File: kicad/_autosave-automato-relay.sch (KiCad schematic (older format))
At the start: 39 parts, among them J1 TE-3-213598-4, J2 Screw_Terminal_01x03, J3 TE-3-213598-4, J4 Screw_Terminal_01x05, J5 TE-3-213598-4, J6 TE-3-213598-4, J7 Screw_Terminal_01x05, J8 TE-3-213598-4, K1 G5LE-14, K2 G5LE-14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

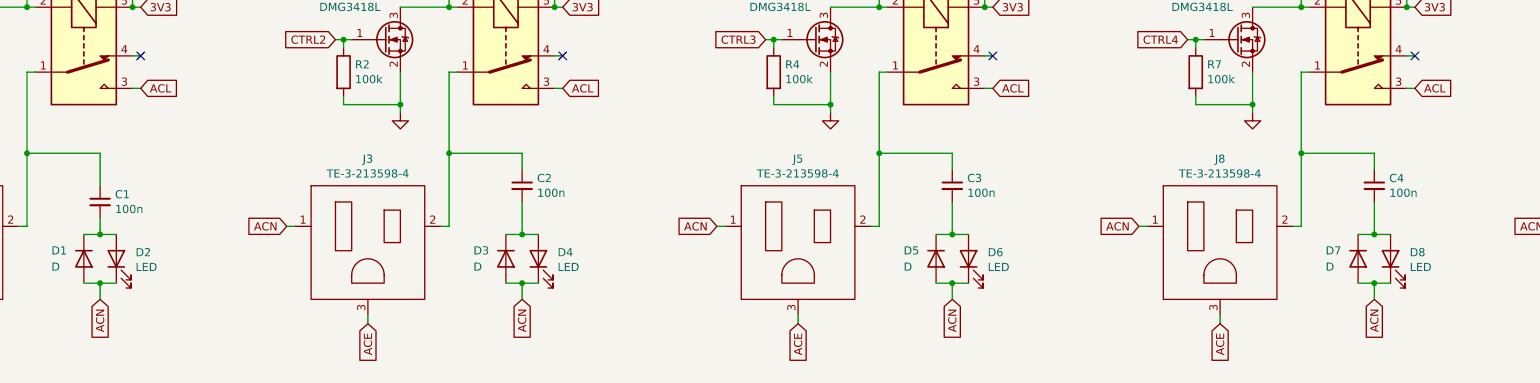
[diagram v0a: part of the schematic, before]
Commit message: Final Rev
Added varistor, poured power planes, added mounting holes, modified data headers, added space for IEC connector.
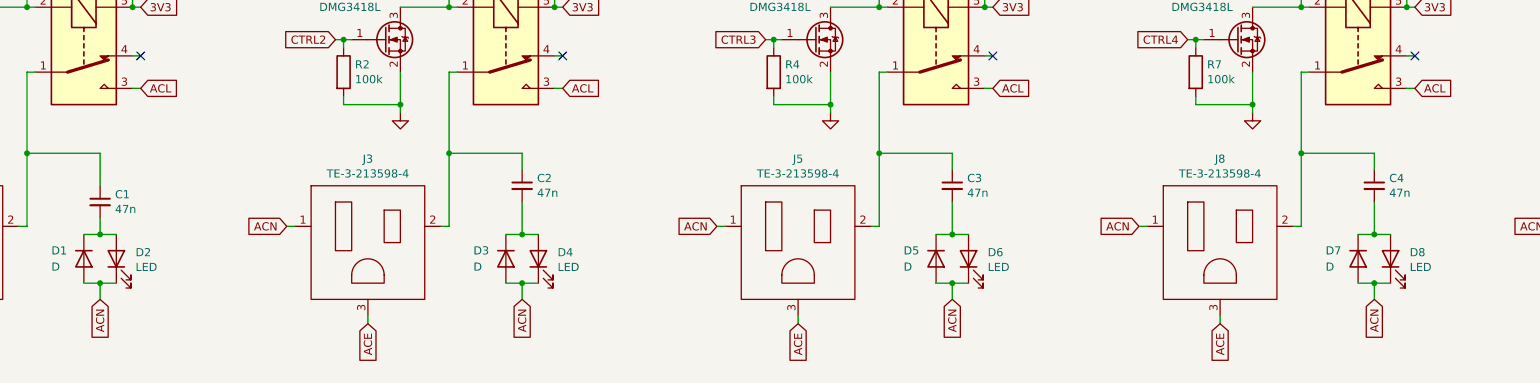
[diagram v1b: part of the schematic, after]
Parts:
- C1, C2, C3, C4: value 100n -> 47n
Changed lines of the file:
@@
 P 2600 5100
 F 0 "C1" H 2692 5146 50  0000 L CNN
-F 1 "100n" H 2692 5055 50  0000 L CNN
+F 1 "47n" H 2692 5055 50  0000 L CNN
 F 2 "Capacitor_SMD:C_1206_3216Metric" H 2600 5100 50  0001 C CNN
 F 3 "~" H 2600 5100 50  0001 C CNN
@@
 P 5200 5000
 F 0 "C2" H 5292 5046 50  0000 L CNN
-F 1 "100n" H 5292 4955 50  0000 L CNN
+F 1 "47n" H 5292 4955 50  0000 L CNN
 F 2 "Capacitor_SMD:C_1206_3216Metric" H 5200 5000 50  0001 C CNN
 F 3 "~" H 5200 5000 50  0001 C CNN
@@
 P 7850 5000
 F 0 "C3" H 7942 5046 50  0000 L CNN
-F 1 "100n" H 7942 4955 50  0000 L CNN
+F 1 "47n" H 7942 4955 50  0000 L CNN
 F 2 "Capacitor_SMD:C_1206_3216Metric" H 7850 5000 50  0001 C CNN
 F 3 "~" H 7850 5000 50  0001 C CNN
@@
 P 10450 5000
 F 0 "C4" H 10542 5046 50  0000 L CNN
-F 1 "100n" H 10542 4955 50  0000 L CNN
+F 1 "47n" H 10542 4955 50  0000 L CNN
 F 2 "Capacitor_SMD:C_1206_3216Metric" H 10450 5000 50  0001 C CNN
 F 3 "~" H 10450 5000 50  0001 C CNN
